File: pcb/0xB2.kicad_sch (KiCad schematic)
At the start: 40 parts, among them J1 USB_C_Receptacle_USB2.0, J2 Conn_01x12, J3 Conn_01x05, J4 Conn_01x12, J5 Conn_01x02, SW1 SW_Push, SW2 SW_Push, U1 RP2040, U2 GD25Q80CEIGR, U3 XC6210B332MR-G, Y1 Crystal_GND24

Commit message: revert to 3.0
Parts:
- J1: footprint 0xLib_USB_Type-C:USB_C_Receptacle_HRO_TYPE-C-31-M-13B -> 0xLib_USB_Type-C:USB_C_Receptacle_HRO_TYPE-C-31-M-14; LCSC C2848619 -> C223907
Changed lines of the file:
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@@
     (property "Reference" "J1" (id 0) (at 35.56 29.21 0))
     (property "Value" "USB_C_Receptacle_USB2.0" (id 1) (at 35.56 31.75 0))
-    (property "Footprint" "0xLib_USB_Type-C:USB_C_Receptacle_HRO_TYPE-C-31-M-13B" (id 2) (at 39.37 52.07 0)
+    (property "Footprint" "0xLib_USB_Type-C:USB_C_Receptacle_HRO_TYPE-C-31-M-14" (id 2) (at 39.37 52.07 0)
       (effects (font (size 1.27 1.27)) hide)
     )
@@
       (effects (font (size 1.27 1.27)) hide)
     )
-    (property "LCSC" "C2848619" (id 4) (at 35.56 52.07 0)
+    (property "LCSC" "C223907" (id 4) (at 35.56 52.07 0)
       (effects (font (size 1.27 1.27)) hide)
     )
@@
     )
     (path "/6125bb34-31fe-49ed-b2ab-61dab24d450a"
-      (reference "J1") (unit 1) (value "USB_C_Receptacle_USB2.0") (footprint "0xLib_USB_Type-C:USB_C_Receptacle_HRO_TYPE-C-31-M-13B")
+      (reference "J1") (unit 1) (value "USB_C_Receptacle_USB2.0") (footprint "0xLib_USB_Type-C:USB_C_Receptacle_HRO_TYPE-C-31-M-14")
     )
     (path "/44683f1e-d2b9-4133-9a9d-84586c32a6a2"

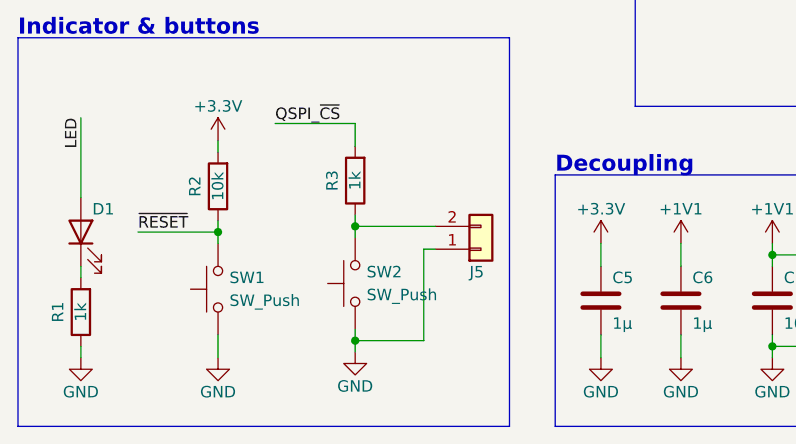
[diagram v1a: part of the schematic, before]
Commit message: change usb c
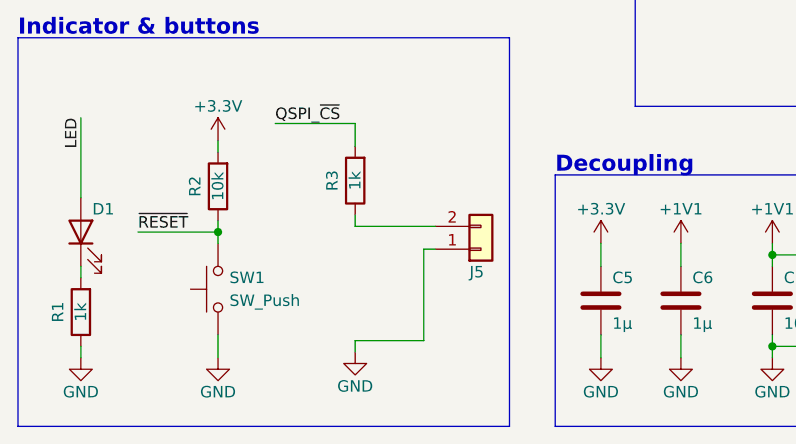
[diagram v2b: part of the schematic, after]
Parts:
- removed SW2: SW_Push, Button_Switch_SMD:SW_SPST_CK_KXT3, symbol Switch:SW_Push
- J1: footprint 0xLib_USB_Type-C:USB_C_Receptacle_HRO_TYPE-C-31-M-14 -> 0xB2_drawings:GT-USB-7014C
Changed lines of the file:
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@@
   (junction (at 71.12 44.45) (diameter 0) (color 0 0 0 0)
   )
-  (junction (at 55.245 172.085) (diameter 0) (color 0 0 0 0)
-  )
   (junction (at 130.81 185.42) (diameter 0) (color 0 0 0 0)
   )
   (junction (at 97.79 106.68) (diameter 0) (color 0 0 0 0)
-  )
-  (junction (at 55.245 184.785) (diameter 0) (color 0 0 0 0)
   )
   (junction (at 33.02 115.57) (diameter 0) (color 0 0 0 0)
@@
     (stroke (width 0) (type default) (color 0 0 0 0))
   )
-  (wire (pts (xy 55.245 172.085) (xy 55.245 173.355))
-    (stroke (width 0) (type default) (color 0 0 0 0))
-  )
   (wire (pts (xy 105.41 90.17) (xy 93.98 90.17))
     (stroke (width 0) (type default) (color 0 0 0 0))
@@
   )
   (wire (pts (xy 76.2 33.02) (xy 76.2 36.83))
-    (stroke (width 0) (type default) (color 0 0 0 0))
-  )
-  (wire (pts (xy 55.245 183.515) (xy 55.245 184.785))
     (stroke (width 0) (type default) (color 0 0 0 0))
   )
@@
     (pin "4")
   )
-  (symbol (lib_id "Switch:SW_Push") (at 55.245 178.435 90) (unit 1)
-    (in_bom yes) (on_board yes) (fields_autoplaced)
-    (property "Reference" "SW2" (id 0) (at 56.515 177.1649 90)
-      (effects (font (size 1.27 1.27)) (justify right))
-    )
-    (property "Value" "SW_Push" (id 1) (at 56.515 179.7049 90)
-      (effects (font (size 1.27 1.27)) (justify right))
-    )
-    (property "Footprint" "Button_Switch_SMD:SW_SPST_CK_KXT3" (id 2) (at 50.165 178.435 0)
-      (effects (font (size 1.27 1.27)) hide)
-    )
-    (property "Datasheet" "~" (id 3) (at 50.165 178.435 0)
-      (effects (font (size 1.27 1.27)) hide)
-    )
-    (property "LCSC" "C319433" (id 4) (at 55.245 178.435 0)
-      (effects (font (size 1.27 1.27)) hide)
-    )
-    (pin "1")
-    (pin "2")
-  )
   (symbol (lib_id "power:GND") (at 40.005 186.69 0) (unit 1)
     (in_bom yes) (on_board yes)
@@
     (property "Reference" "J1" (id 0) (at 35.56 29.21 0))
     (property "Value" "USB_C_Receptacle_USB2.0" (id 1) (at 35.56 31.75 0))
-    (property "Footprint" "0xLib_USB_Type-C:USB_C_Receptacle_HRO_TYPE-C-31-M-14" (id 2) (at 39.37 52.07 0)
+    (property "Footprint" "0xB2_drawings:GT-USB-7014C" (id 2) (at 39.37 52.07 0)
       (effects (font (size 1.27 1.27)) hide)
     )
@@
     )
     (path "/6125bb34-31fe-49ed-b2ab-61dab24d450a"
-      (reference "J1") (unit 1) (value "USB_C_Receptacle_USB2.0") (footprint "0xLib_USB_Type-C:USB_C_Receptacle_HRO_TYPE-C-31-M-14")
+      (reference "J1") (unit 1) (value "USB_C_Receptacle_USB2.0") (footprint "0xB2_drawings:GT-USB-7014C")
     )
     (path "/44683f1e-d2b9-4133-9a9d-84586c32a6a2"
@@
       (reference "SW1") (unit 1) (value "SW_Push") (footprint "Button_Switch_SMD:SW_SPST_CK_KXT3")
     )
-    (path "/4ea9bd29-a5a9-4d62-b350-c59ad41d14d5"
-      (reference "SW2") (unit 1) (value "SW_Push") (footprint "Button_Switch_SMD:SW_SPST_CK_KXT3")
-    )
     (path "/073e7a20-6222-4c9d-9f89-871bf718b9fb"
